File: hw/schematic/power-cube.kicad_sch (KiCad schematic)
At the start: 50 parts, among them J1 Conn_01x03, J2 Conn_01x04, M1 INA226-MOD, M2 HUSB238-USBPD, M3 USBC-MOD, M4 WEACT-STM32G474, M5 BlueM-D100, M6 BMP280-MOD, Q1 IRF7404, Q2 IRF7404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

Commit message: mod schematic
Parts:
- C1, C4: value 10uF -> 1uF
- C3, C5: value 1uF -> 1000pF
- L1: footprint Inductor_SMD:L_2512_6332Metric_Pad1.52x3.35mm_HandSolder -> Inductor_THT:L_Axial_L5.3mm_D2.2mm_P10.16mm_Horizontal_Vishay_IM-1
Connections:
- net +3V3: now also D2.2 (A), R2.1, R3.1
- net GND: now also C1.1, C4.1
- net VCC: no longer D2.2 (A), R2.1, R3.1
- net VDD: no longer R6.1
- net at C2.1, C3.1, Q1.4 (G)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: no longer C1.1
- net at C5.1, Q4.4 (G), R10.2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: no longer C4.1
- net VDC: now reaches C5.2, D6.2 (A), Q4.5 (D), Q4.6 (D), Q4.7 (D), Q4.8 (D)
- net VDC: now also R6.1
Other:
- moved on the sheet: D6, R6, R8

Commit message: add source
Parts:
- added R20: 47K, Resistor_SMD:R_0805_2012Metric_Pad1.20x1.40mm_HandSolder, symbol Device:R
- R18, R19, R2, R3: value 1K -> N.C.
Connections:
- net EN_EXTRAPWR: now also R20.2
- net GND: now also R20.1
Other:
- moved on the sheet: C9, M6, R18, R19, U1

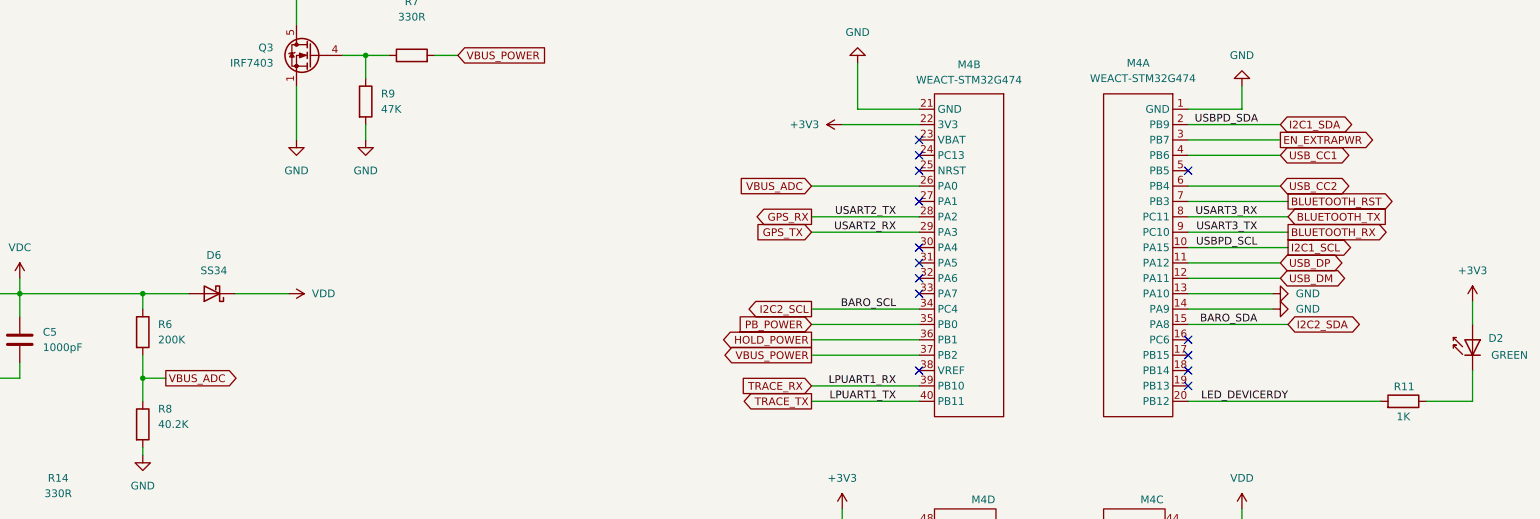
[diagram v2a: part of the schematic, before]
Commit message: use message-q
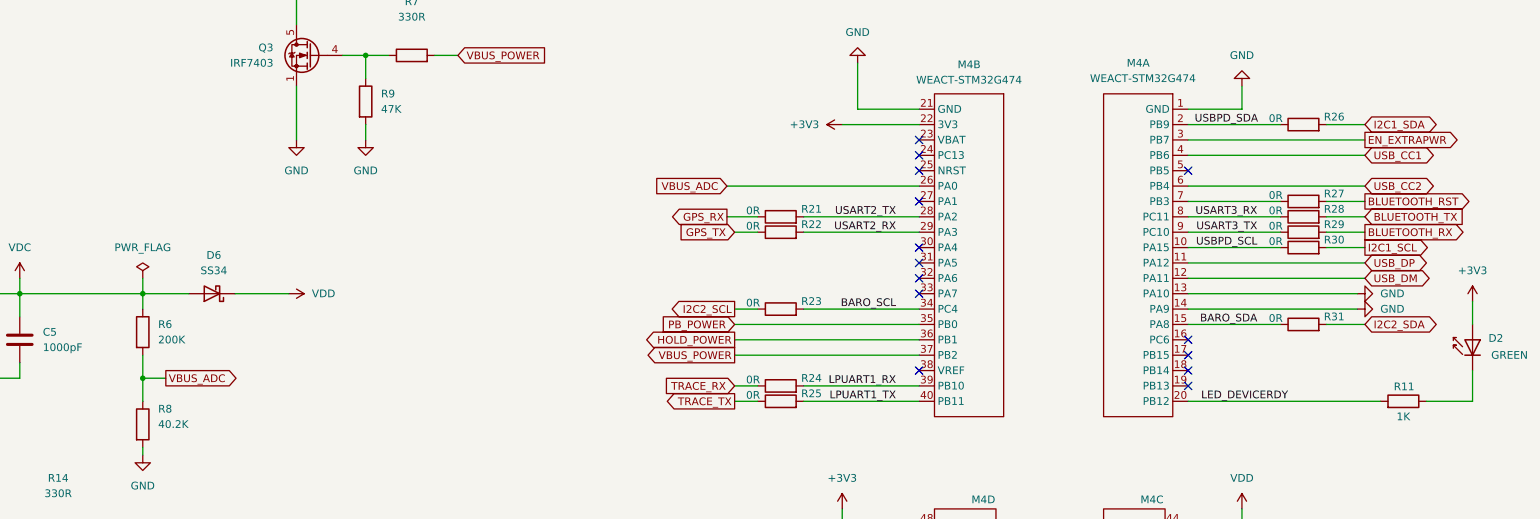
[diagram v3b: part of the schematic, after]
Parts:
- added R21, R22, R23, R24, R25, R26, R27, R28, R29, R30, R31: 0R, Resistor_SMD:R_0805_2012Metric_Pad1.20x1.40mm_HandSolder, symbol Device:R
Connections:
- net BLUETOOTH_RST: now also R27.2; no longer M4.7 (PB3)
- net BLUETOOTH_RX: now also R29.2; no longer M4.9 (PC10)
- net BLUETOOTH_TX: now also R28.2; no longer M4.8 (PC11)
- net GPS_RX: now also R21.1; no longer M4.28 (PA2)
- net GPS_TX: now also R22.1; no longer M4.29 (PA3)
- net I2C1_SCL: now also R30.2; no longer M4.10 (PA15)
- net I2C1_SDA: now also R26.2; no longer M4.2 (PB9)
- net I2C2_SCL: now also R23.1; no longer M4.34 (PC4)
- net I2C2_SDA: now also R31.2; no longer M4.15 (PA8)
- net TRACE_RX: now also R24.1; no longer M4.39 (PB10)
- net TRACE_TX: now also R25.1; no longer M4.40 (PB11)
- new net: M4.7 (PB3), R27.1
- new net BARO_SCL: M4.34 (PC4), R23.2
- new net BARO_SDA: M4.15 (PA8), R31.1
- new net LPUART1_RX: M4.39 (PB10), R24.2
- new net LPUART1_TX: M4.40 (PB11), R25.2
- new net USART2_RX: M4.29 (PA3), R22.2
- new net USART2_TX: M4.28 (PA2), R21.2
- new net USART3_RX: M4.8 (PC11), R28.1
- new net USART3_TX: M4.9 (PC10), R29.1
- new net USBPD_SCL: M4.10 (PA15), R30.1
- new net USBPD_SDA: M4.2 (PB9), R26.1
